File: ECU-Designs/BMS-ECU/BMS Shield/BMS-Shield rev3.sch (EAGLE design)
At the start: 41 parts, among them J1 ARDUINO_R3_SHIELD, X1 CONNECTOR-4

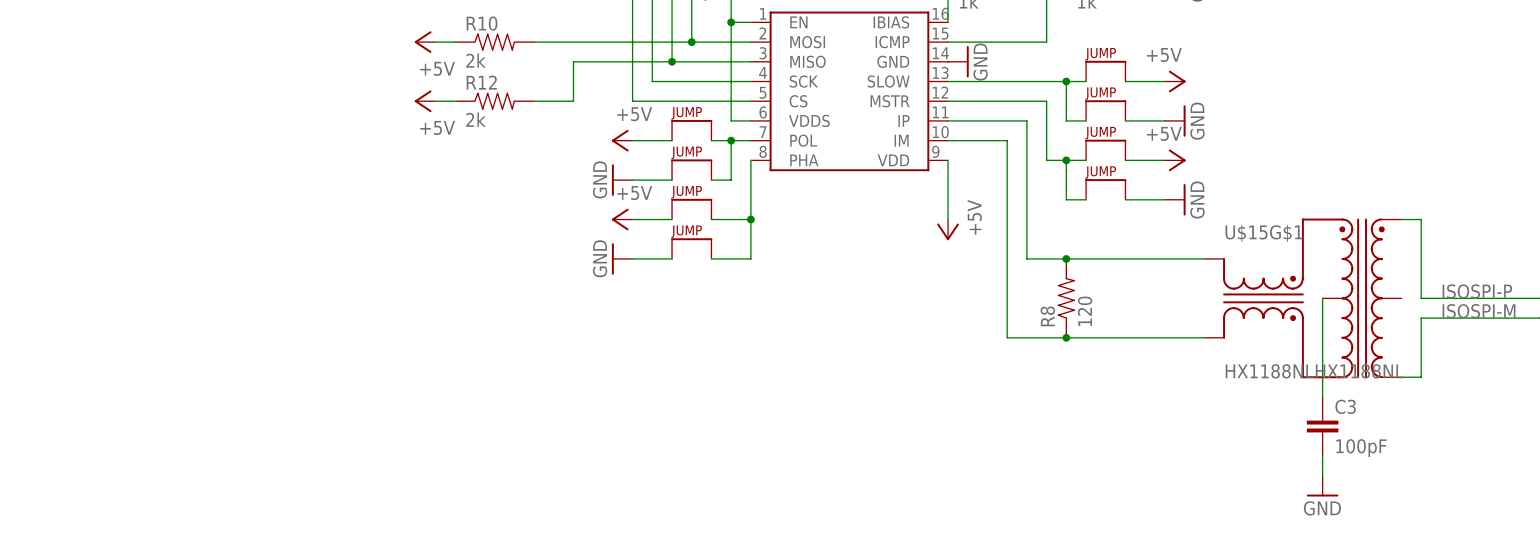
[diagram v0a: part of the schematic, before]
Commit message: New versions of power board, bspd test board, can shield, bms adapter segment, bms shield
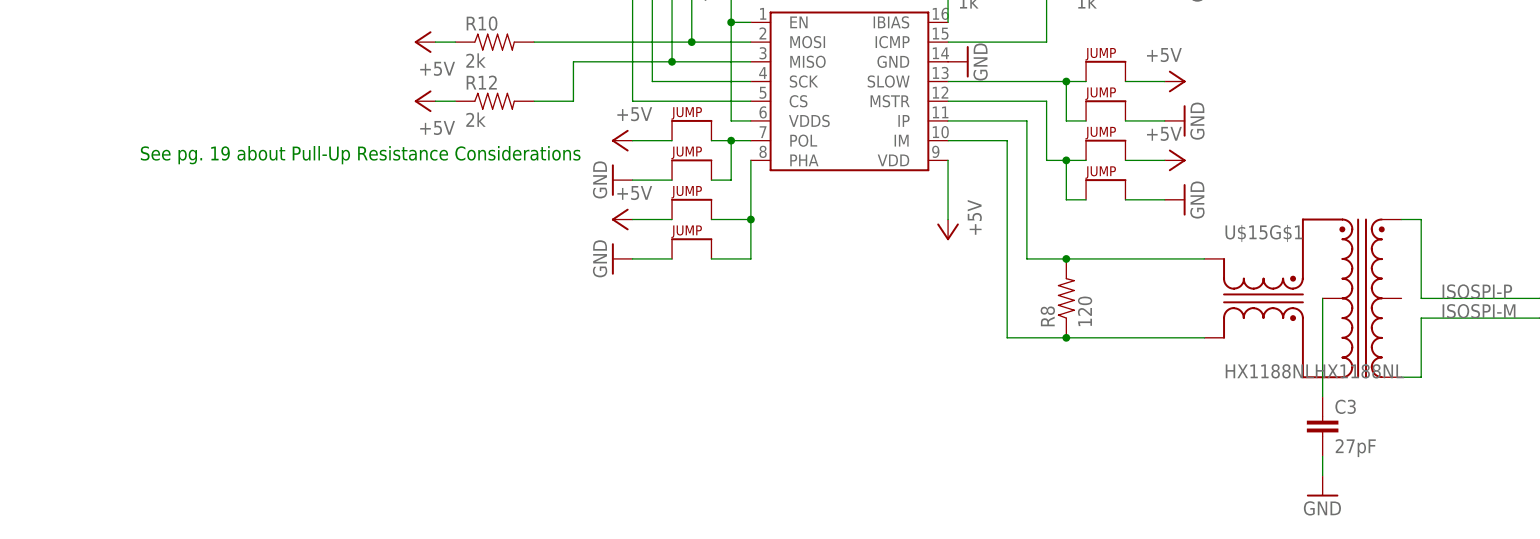
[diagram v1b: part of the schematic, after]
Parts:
- C3: value 100pF -> 27pF
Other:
- note added: "See pg. 19 about Pull-Up Resistance Considerations"
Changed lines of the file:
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@@
 <part name="GND15" library="HyTechSymbols" deviceset="GND" device=""/>
 <part name="R8" library="HyTechDevices" deviceset="RESISTOR" device="0805-RES" value="120"/>
-<part name="C3" library="HyTechDevices" deviceset="CAP" device="0805" value="100pF"/>
+<part name="C3" library="HyTechDevices" deviceset="CAP" device="0805" value="27pF"/>
 <part name="ISOSPI" library="HyTechDevices" deviceset="CONNECTOR-2" device=""/>
 <part name="GND16" library="HyTechSymbols" deviceset="GND" device=""/>
@@
 <plain>
 <text x="0" y="30.48" size="1.778" layer="97">Cut one of these inputs ➡️</text>
+<text x="10.16" y="-12.7" size="1.778" layer="91">See pg. 19 about Pull-Up Resistance Considerations</text>
 </plain>
 <instances>
